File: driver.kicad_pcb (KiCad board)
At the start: 2 copper layers, 53.8 x 69.1 mm, 53 parts, among them J1 Screw_Terminal_01x02, J2 Conn_02x16_Odd_Even, Q1 Q_NMOS_GDSD, Q10 Q_NMOS_GDSD, Q11 Q_NMOS_GDSD, Q12 Q_NMOS_GDSD, Q13 Q_NMOS_GDSD, Q14 Q_NMOS_GDSD, Q15 Q_NMOS_GDSD, Q16 Q_NMOS_GDSD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

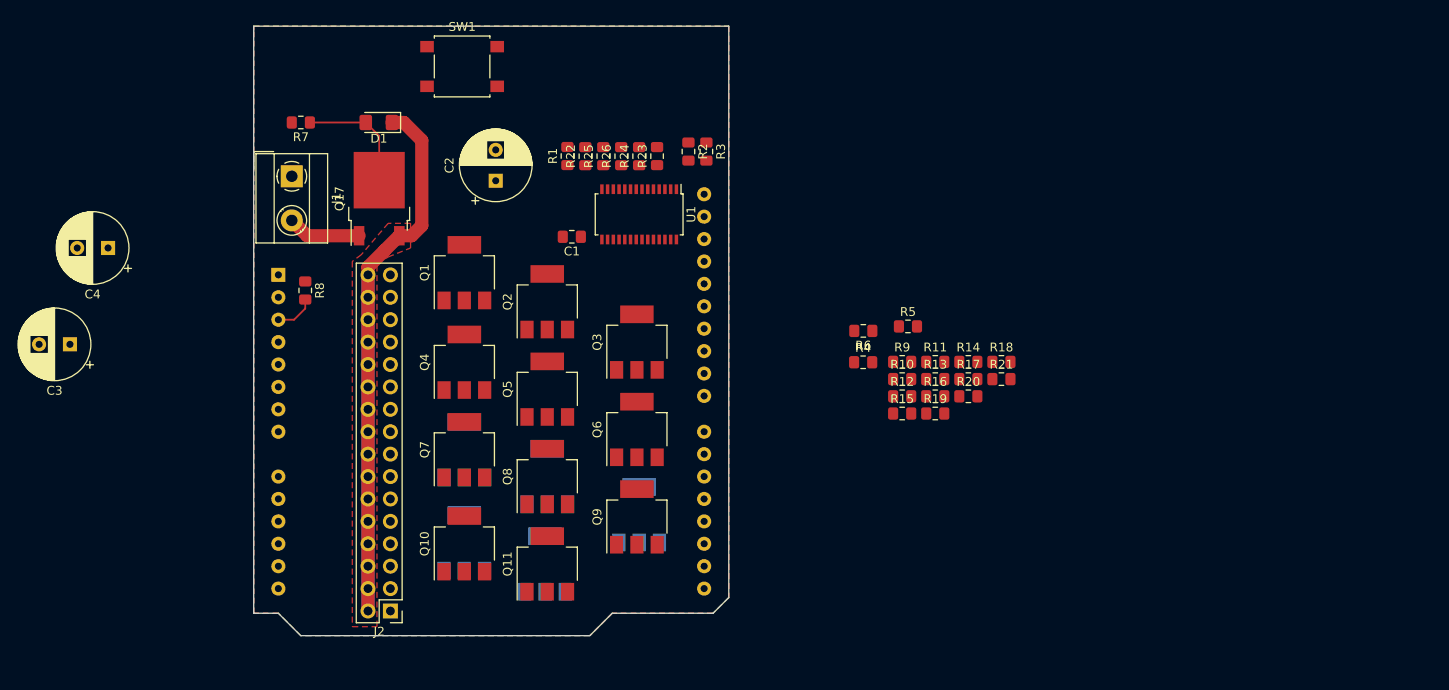
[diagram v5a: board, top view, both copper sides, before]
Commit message: Change all resistors to 10K 0805. More routing and placement
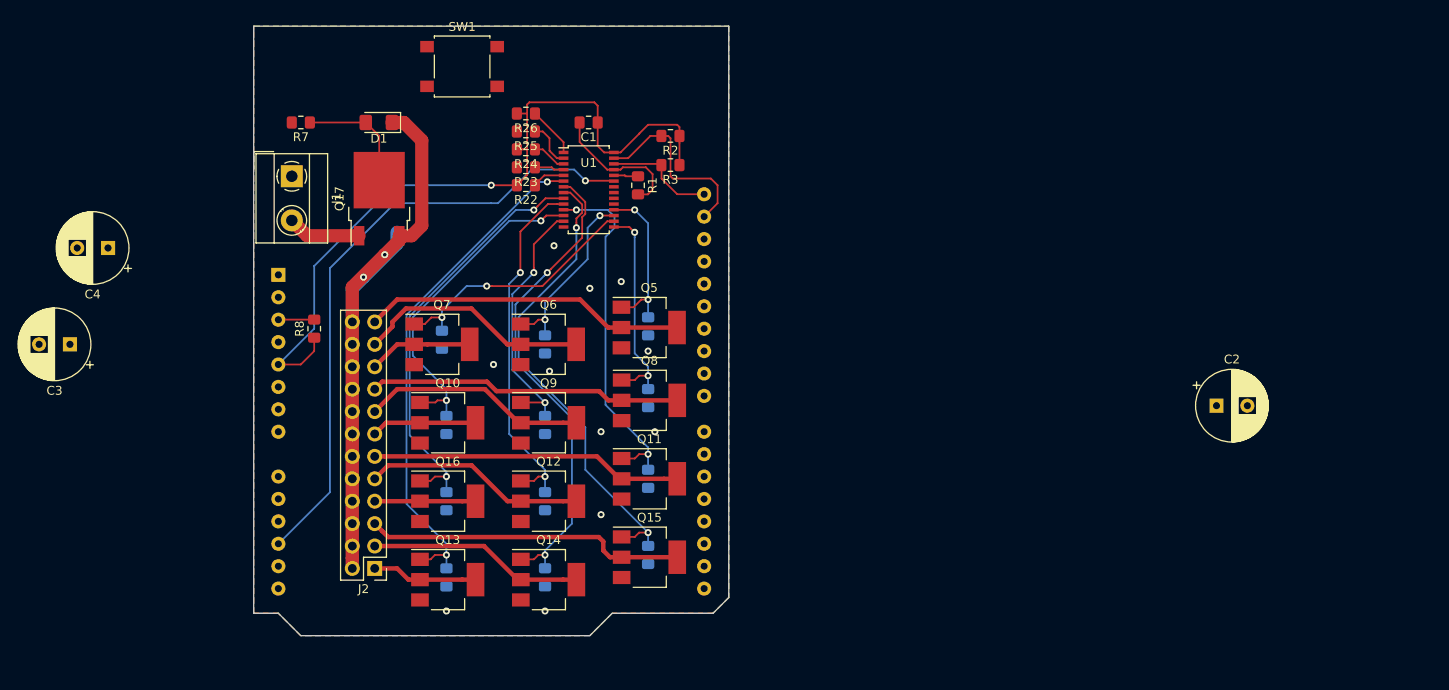
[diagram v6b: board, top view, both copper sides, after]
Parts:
- removed Q1, Q2, Q3, Q4: Q_NMOS_GDSD, Package_TO_SOT_SMD:SOT-223
- removed R14, R15, R16, R17: 10k, Resistor_SMD:R_0805_2012Metric_Pad1.15x1.40mm_HandSolder
- J2: value Conn_02x16_Odd_Even -> Conn_02x12_Odd_Even; footprint Connector_PinHeader_2.54mm:PinHeader_2x16_P2.54mm_Vertical -> Connector_PinHeader_2.54mm:PinHeader_2x12_P2.54mm_Vertical
- Q12, Q13, Q14, Q15, Q16: moved to F.Cu
- R1, R22, R23, R24, R25, R26, R8: value 1K -> 10K
- R10, R11, R12, R13, R18, R19, R20, R21, R4, R5, R6, R9: value 10k -> 10K; moved to B.Cu
- R2, R3: value 10k -> 10K
- moved C2 85.6 mm to (184.3, 116.2), turned to 0 degrees
- moved R20 60.0 mm to (96.5, 108.7), turned to 270 degrees
- moved R9 54.0 mm to (97.0, 127.0), turned to 270 degrees
- moved R4 53.2 mm to (97.0, 135.6), turned to 270 degrees
- moved R12 51.8 mm to (97.0, 118.4), turned to 270 degrees
- moved R5 50.0 mm to (108.2, 135.6), turned to 270 degrees
- moved R19 44.9 mm to (108.2, 109.2), turned to 270 degrees
- moved R13 44.5 mm to (108.2, 118.4), turned to 270 degrees
- moved R10 42.8 mm to (108.2, 127.0), turned to 270 degrees
- moved R18 40.3 mm to (119.9, 107.2), turned to 270 degrees
- moved R21 40.1 mm to (119.9, 115.3), turned to 270 degrees
- moved R6 35.2 mm to (119.9, 133.1), turned to 270 degrees
- moved R11 35.1 mm to (119.9, 124.5), turned to 270 degrees
- moved Q11 15.1 mm to (120.0, 124.5), turned to 0 degrees
- moved R23 14.9 mm to (106.0, 89.2), turned to 180 degrees
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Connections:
- U1 pad 19: /PWM12 -> Net-(U1-Pad19)
- U1 pad 20: /PWM13 -> Net-(U1-Pad20)
- U1 pad 21: /PWM14 -> Net-(U1-Pad21)
- U1 pad 22: /PWM15 -> Net-(U1-Pad22)
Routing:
- net VCC: track 0.00 -> 85.9 mm, vias 0 -> 1
- net /~OE: track 0.00 -> 71.0 mm, vias 0 -> 1
- net /PWM0: track 0.00 -> 58.2 mm, vias 0 -> 2
- net /PWM1: track 0.00 -> 54.8 mm, vias 0 -> 2
- net /PWM2: track 0.00 -> 53.6 mm, vias 0 -> 2
- net /PWM3: track 0.00 -> 47.9 mm, vias 0 -> 2
- net /PWM4: track 0.00 -> 40.9 mm, vias 0 -> 2
- net /PWM5: track 0.00 -> 40.4 mm, vias 0 -> 2
- net /PWM6: track 0.00 -> 37.7 mm, vias 0 -> 2
- net PWR_CH11: track 0.00 -> 36.6 mm
- net PWR_CH2: track 0.00 -> 36.5 mm
- net PWR_CH8: track 0.00 -> 35.5 mm
- net PWR_CH5: track 0.00 -> 35.3 mm
- net /PWM9: track 0.00 -> 29.4 mm, vias 0 -> 2
- net /PWM7: track 0.00 -> 29.2 mm, vias 0 -> 2
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- removed copper zone on F.Cu, net (none)

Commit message: replace zener with voltage divdier, swap MOSFETs, update footprints, separate power and signal ground planes
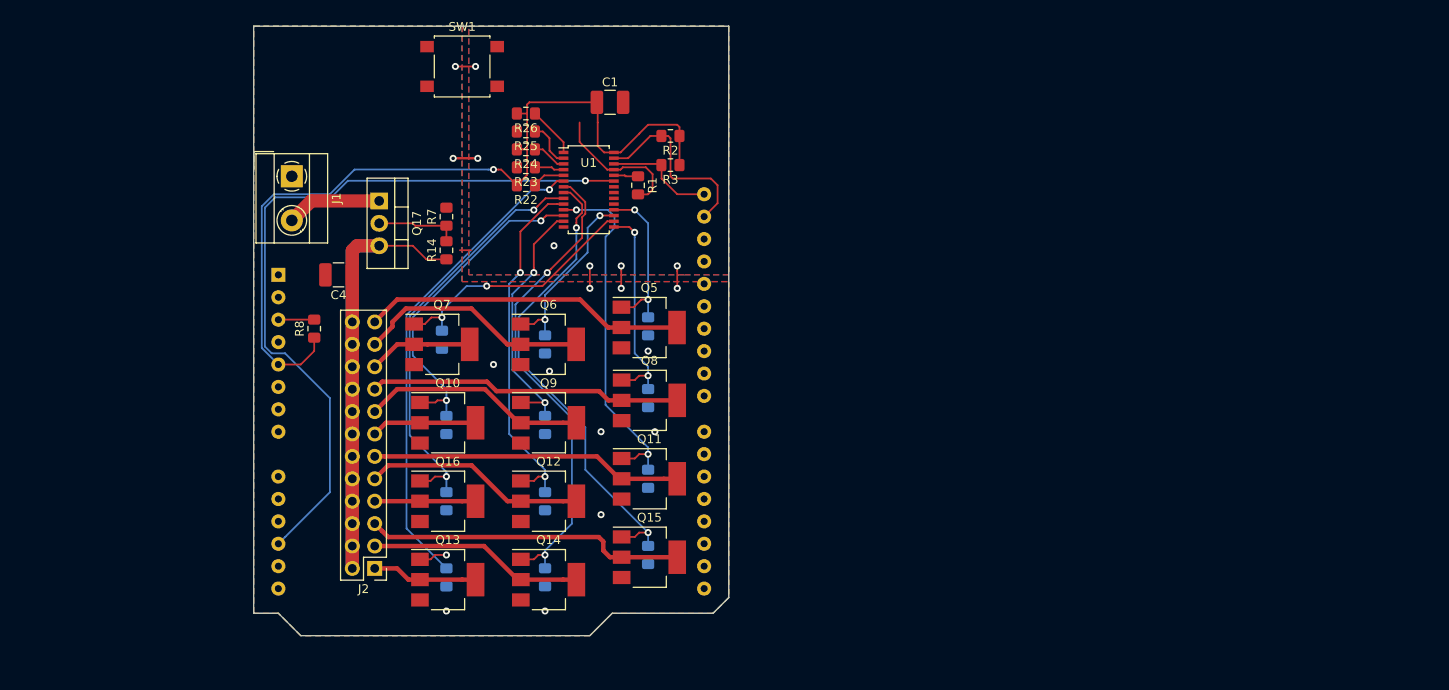
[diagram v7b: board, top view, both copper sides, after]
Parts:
- removed C2: 100uF, Capacitor_THT:CP_Radial_D8.0mm_P3.50mm
- removed C3: CP, Capacitor_THT:CP_Radial_D8.0mm_P3.50mm
- removed D1: Zener 10V, Diode_SMD:D_1206_3216Metric_Pad1.42x1.75mm_HandSolder
- added R14: 10K, Resistor_SMD:R_0805_2012Metric_Pad1.15x1.40mm_HandSolder, F.Cu at (97.0, 98.6)
- C1: value 1u -> 0.1uF; footprint Capacitor_SMD:C_0805_2012Metric_Pad1.15x1.40mm_HandSolder -> Capacitor_SMD:C_1210_3225Metric_Pad1.42x2.65mm_HandSolder
- C4: value C -> 0.1uF 60V; footprint Capacitor_THT:CP_Radial_D8.0mm_P3.50mm -> Capacitor_SMD:C_1210_3225Metric_Pad1.42x2.65mm_HandSolder
- Q17: value AOD417 Q_PMOS_DGS -> IRF9Z34 PMOS_DGS; footprint Package_TO_SOT_SMD:TO-252-2 -> Package_TO_SOT_THT:TO-220-3_Vertical
- R7: value 10K -> 18K
- moved C4 26.3 mm to (84.8, 101.3)
- moved R7 19.7 mm to (97.0, 94.8), turned to 90 degrees
- moved C1 3.33 mm to (115.6, 81.8), turned to 0 degrees
- moved Q17 0.25 mm to (89.4, 93.0), turned to 270 degrees
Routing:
- net GND: track 15.9 -> 32.2 mm, vias 11 -> 19
- net /~OE: track 71.0 -> 85.3 mm
- net VCC: track 85.9 -> 96.4 mm
- net 28V: track 97.0 -> 86.9 mm, vias 2 -> 0
- net Net-(Q17-Pad2): track 13.5 -> 9.49 mm
- net /input_hicurrent: track 8.35 -> 10.8 mm

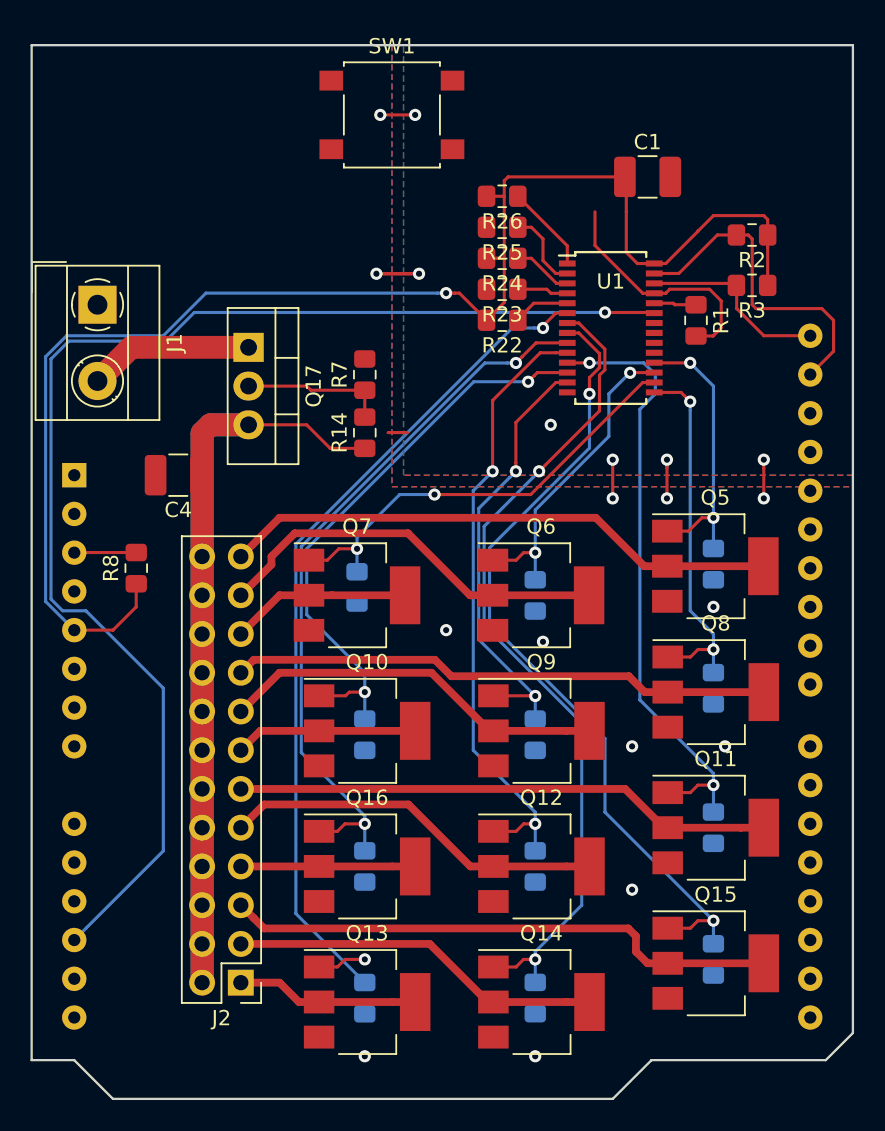
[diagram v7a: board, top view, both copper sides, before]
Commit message: Capacitor updates + voltage limit 50V + routing
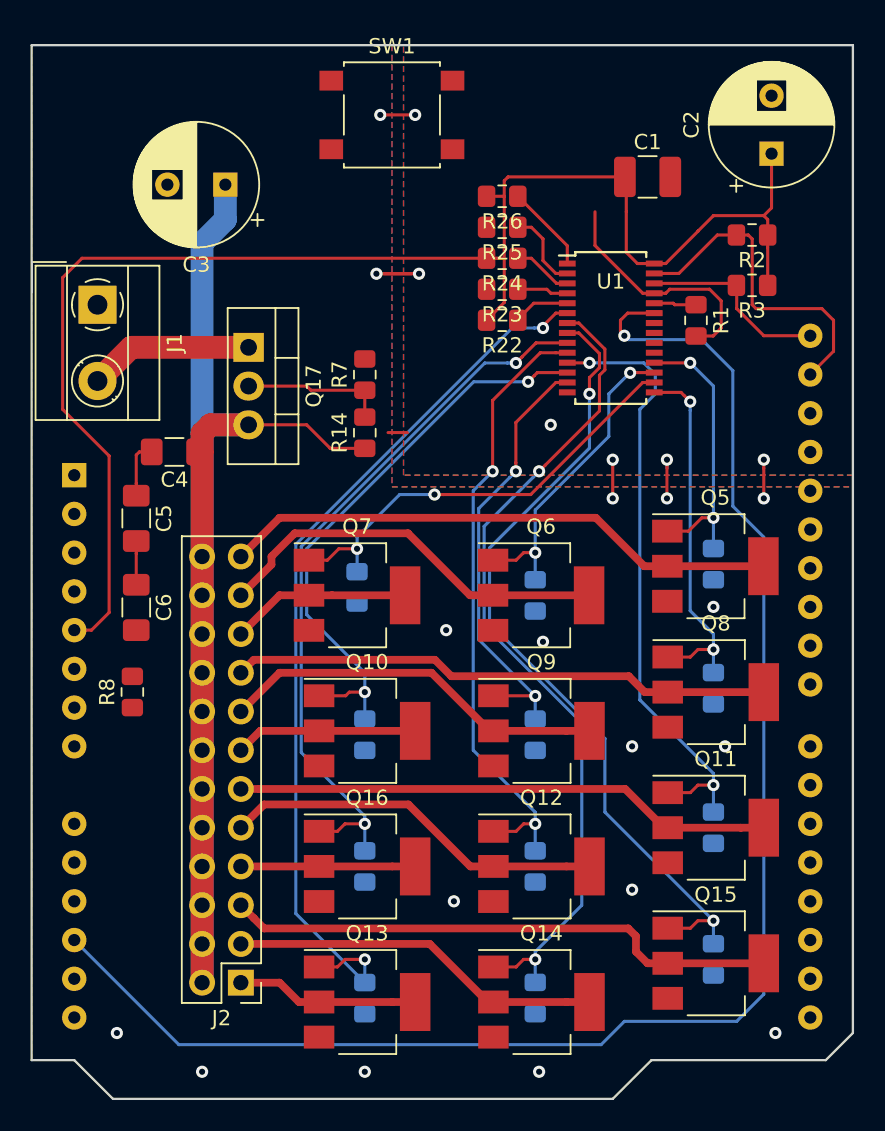
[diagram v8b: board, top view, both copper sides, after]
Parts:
- added C2: 1uF, Capacitor_THT:CP_Radial_D8.0mm_P3.80mm, F.Cu at (123.7, 80.3)
- added C3: 1uF 60V, Capacitor_THT:CP_Radial_D8.0mm_P3.80mm, F.Cu at (87.9, 82.3)
- added C5: 1uF 25V, Capacitor_SMD:C_1206_3216Metric_Pad1.42x1.75mm_HandSolder, F.Cu at (82.0, 104.2)
- added C6: 1uF 25V, Capacitor_SMD:C_1206_3216Metric_Pad1.42x1.75mm_HandSolder, F.Cu at (82.0, 110.0)
- C4: value 0.1uF 60V -> 1uF 25V; footprint Capacitor_SMD:C_1210_3225Metric_Pad1.42x2.65mm_HandSolder -> Capacitor_SMD:C_1206_3216Metric_Pad1.42x1.75mm_HandSolder
- moved R8 8.12 mm to (81.8, 115.6)
- moved C4 1.55 mm to (84.5, 99.8)
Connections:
- C4 pad 2: GND -> Net-(C4-Pad2)
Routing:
- net /~OE: track 85.3 -> 102.7 mm
- net 28V: track 86.9 -> 103.8 mm
- net Net-(A1-Pad3): track 4.07 -> 0.00 mm
- net Net-(C4-Pad2): track 0.00 -> 3.76 mm
- net Net-(C5-Pad2): track 0.00 -> 2.87 mm
- net VCC: track 96.4 -> 98.7 mm, vias 1 -> 0
- net /PWM0: track 58.3 -> 59.8 mm
- net GND: vias 19 -> 23
